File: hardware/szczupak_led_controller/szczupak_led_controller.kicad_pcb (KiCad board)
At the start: 4 copper layers, 123 parts, among them IC1 STM32G0B1CBT6, IC2 SN65HVD230DR, IC3 TLV75533PDBVR, J1 Conn_01x05, J10 XT60PW-M, J2 USB4110-GF-A, J3 CAN_CONN, J4 43650-0200, J5 43650-0300, J6 CAN_CONN, J7 Conn_EXT, J8 XT60PW-M, J9 XT60PW-M, Q1 AO4407A, Q2 AO3401A, Q3 2N7002, Q4 2N7002, Q5 2N7002, U1 USBLC6-2SC6, U3 3568

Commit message: #8 Finished initial component placement on pcb
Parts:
- removed C23, C35: 47pF DNP, Capacitor_SMD:C_0603_1608Metric
- removed D13: PESD1CAN,215, szczupak_led_controller:SOT95P230X110-3N
- added REF**: MountingHole_3.2mm_M3, MountingHole:MountingHole_3.2mm_M3, F.Cu at (83.5, 126.5)
- added REF**: MountingHole_3.2mm_M3, MountingHole:MountingHole_3.2mm_M3, F.Cu at (153.0, 73.0)
- added REF**: MountingHole_3.2mm_M3, MountingHole:MountingHole_3.2mm_M3, F.Cu at (85.5, 63.0)
- added REF**: MountingHole_3.2mm_M3, MountingHole:MountingHole_3.2mm_M3, F.Cu at (85.0, 85.5)
- added REF**: MountingHole_3.2mm_M3, MountingHole:MountingHole_3.2mm_M3, F.Cu at (164.0, 126.0)
- added REF**: MountingHole_3.2mm_M3, MountingHole:MountingHole_3.2mm_M3, F.Cu at (153.0, 95.5)
- C21, C24, C29, C30, C33, C34: moved to F.Cu
- C22, C5, F2, F3, F4, R23, R24, R25, R26: moved to B.Cu
- J7: footprint Connector_PinHeader_2.54mm:PinHeader_1x08_P2.54mm_Vertical -> Connector_PinHeader_2.54mm:PinHeader_1x10_P2.54mm_Vertical
- moved R14 268.4 mm to (86.5, 98.5), turned to -90 degrees
- moved IC3 266.4 mm to (101.6, 107.1), turned to -90 degrees
- moved D6 265.8 mm to (96.0, 102.5), turned to 180 degrees
- moved D9 265.5 mm to (96.1, 106.0), turned to 180 degrees
- moved J7 258.9 mm to (86.4, 53.0), turned to 90 degrees
- moved C16 258.3 mm to (96.0, 93.7), turned to -90 degrees
- moved C15 256.5 mm to (94.0, 93.7), turned to -90 degrees
- moved C10 256.1 mm to (100.6, 102.1), turned to 90 degrees
- moved R26 255.7 mm to (102.0, 57.5), turned to 90 degrees
- moved C6 255.7 mm to (102.8, 102.1), turned to 90 degrees
- moved C7 253.7 mm to (105.6, 108.6)
- moved C8 253.6 mm to (105.6, 111.1)
- moved R25 253.1 mm to (104.5, 57.5), turned to 90 degrees
- moved D3 252.4 mm to (113.0, 110.7), turned to 90 degrees
- moved D10 248.6 mm to (116.0, 110.7), turned to 90 degrees
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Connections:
- C15 pad 1: +3.3V -> unconnected-(C15-Pad1)
- C15 pad 2: GND -> unconnected-(C15-Pad2)
- C16 pad 1: +3.3V -> unconnected-(C16-Pad1)
- C16 pad 2: GND -> unconnected-(C16-Pad2)
- C5 pad 1: /02_mcu/NRST -> /NRST
- IC1 pad 10: /02_mcu/NRST -> /NRST
- IC1 pad 36: /02_mcu/SWCLK_BOOT0 -> /SWCLK_BOOT0
- J1 pad 1: /02_mcu/SWCLK_BOOT0 -> /SWCLK_BOOT0
- J1 pad 4: /02_mcu/NRST -> /NRST
- J7 pad 3: /USART1_TX -> /SWCLK_BOOT0
- J7 pad 4: /USART1_RX -> /NRST
- J7 pad 5: /I2C1_SDA -> /USART1_TX
- J7 pad 6: /I2C1_SCL -> /USART1_RX
- J7 pad 7: /GPIO_EXT -> /I2C1_SDA
- J7 pad 8: /PWM_EXT -> /I2C1_SCL
- Q4 pad 1: GND -> Net-(Q4-Pad1)
- R1 pad 2: /02_mcu/NRST -> /NRST
- R2 pad 1: /02_mcu/SWCLK_BOOT0 -> /SWCLK_BOOT0
- R32 pad 2: GND -> Net-(Q4-Pad1)
- R34 pad 2: GND -> Net-(Q4-Pad1)
- R7 pad 1: /ADC_LED1 -> Net-(FL1-OUT)
- R7 pad 2: Net-(FL1-OUT) -> /ADC_LED1
- S1 pad 2: /02_mcu/SWCLK_BOOT0 -> /SWCLK_BOOT0
- S1 pad 3: /02_mcu/SWCLK_BOOT0 -> /SWCLK_BOOT0
- S2 pad 1: /02_mcu/NRST -> /NRST
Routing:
- net (no net): track 1.50 -> 0.00 mm

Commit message: #8 Added routing for usb and mcu. Started pouring of power elements
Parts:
- C22, C5, R23, R24: moved to F.Cu
- R12, R13: moved to B.Cu
- moved R12 13.4 mm to (120.1, 68.2)
- moved R13 13.4 mm to (120.1, 66.6)
- moved R24 10.2 mm to (91.8, 64.9), turned to -90 degrees
- moved R23 8.25 mm to (91.8, 68.2), turned to -90 degrees
- moved JP3 8.17 mm to (79.5, 120.8), turned to 0 degrees
- moved C3 6.53 mm to (108.7, 76.0)
- moved C4 6.53 mm to (108.7, 78.0)
- moved C20 5.62 mm to (77.8, 85.5)
- moved C29 4.25 mm to (130.0, 76.8)
- moved C24 4.23 mm to (130.0, 98.8)
- moved C30 4.14 mm to (132.0, 75.0)
- moved C21 3.93 mm to (132.0, 97.5)
- moved C33 3.75 mm to (130.0, 54.0)
- moved C9 3.64 mm to (108.8, 63.9), turned to 90 degrees
- moved R2 3.58 mm to (97.7, 77.4), turned to -90 degrees
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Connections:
- net Net-(D1-K) renamed /02_mcu/LED_STATUS_R
- net Net-(D2-K) renamed /02_mcu/LED_FAULT_R
- net Net-(FL1-OUT) renamed /04_power_output/ADC_R1
- net Net-(FL2-OUT) renamed /04_power_output/ADC_R2
- net Net-(FL3-OUT) renamed /04_power_output/ADC_R3
- net Net-(JP2-A) renamed /03_interfaces/CAN_SHIELD_1
- net Net-(JP3-A) renamed /03_interfaces/CAN_SHIELD_2
- net Net-(Q3-Pad1) renamed /04_power_output/PWM_LED1_GATE
- net Net-(Q4-Pad1) renamed /04_power_output/PWM_LED2_GATE
- net Net-(Q5-Pad1) renamed /04_power_output/PWM_LED3_GATE
- C15 pad 1: unconnected-(C15-Pad1) -> +3.3V
- C15 pad 2: unconnected-(C15-Pad2) -> GND
- C16 pad 1: unconnected-(C16-Pad1) -> +3.3V
- C16 pad 2: unconnected-(C16-Pad2) -> GND
- J7 pad 10: /PWM_EXT -> /GPIO_EXT
- J7 pad 9: /GPIO_EXT -> /PWM_EXT
- S1 pad 5: GND -> unconnected-(S1-GROUND-Pad5)
- S2 pad 5: GND -> unconnected-(S2-GROUND-Pad5)
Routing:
- net /NRST: track 0.00 -> 65.9 mm, vias 0 -> 2
- net /PWM_LED1: track 0.00 -> 65.1 mm, vias 0 -> 2
- net /SWCLK_BOOT0: track 0.00 -> 64.8 mm, vias 0 -> 4
- net /03_interfaces/CAN_P: track 0.00 -> 46.8 mm, vias 0 -> 5
- net /03_interfaces/CAN_N: track 0.00 -> 45.1 mm
- net /PWM_LED2: track 0.00 -> 44.5 mm, vias 0 -> 2
- net /ADC_LED1: track 0.17 -> 40.2 mm
- net /02_mcu/LED_STATUS: track 0.24 -> 34.3 mm, vias 0 -> 2
- net /I2C1_SDA: track 0.00 -> 32.3 mm, vias 0 -> 2
- net /I2C1_SCL: track 0.00 -> 31.8 mm, vias 0 -> 2
- net /03_interfaces/CAN_SPLIT: track 0.00 -> 31.3 mm, vias 0 -> 1
- net /02_mcu/LED_FAULT: track 0.00 -> 31.2 mm, vias 0 -> 2
- net /CAN_TX: track 0.00 -> 31.1 mm
- net /USART1_TX: track 0.00 -> 29.8 mm, vias 0 -> 1
- net /USART1_RX: track 0.00 -> 28.9 mm, vias 0 -> 1
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- added copper zone on B.Cu, net +3.3V
- added copper zone on F.Cu, net +3.3V
- added copper zone on F.Cu, net /01_power_input/12V_FUSE
- added copper zone on F.Cu, net /01_power_input/5V_FUSE
- added copper zone on F.Cu, net /01_power_input/5V_IN
- added copper zone on F.Cu, net /01_power_input/5V_PROT
- added copper zone on F.Cu, net /01_power_input/Q1_GATE
- added copper zone on F.Cu, net /01_power_input/Q2_GATE
- added copper zone on F.Cu, net /04_power_output/12V_CH3
- added copper zone on F.Cu, net /USB_5V
- added copper zone on B.Cu, net GND
- added copper zone on In1.Cu, net GND
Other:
- board outline added: 100 x 83 mm

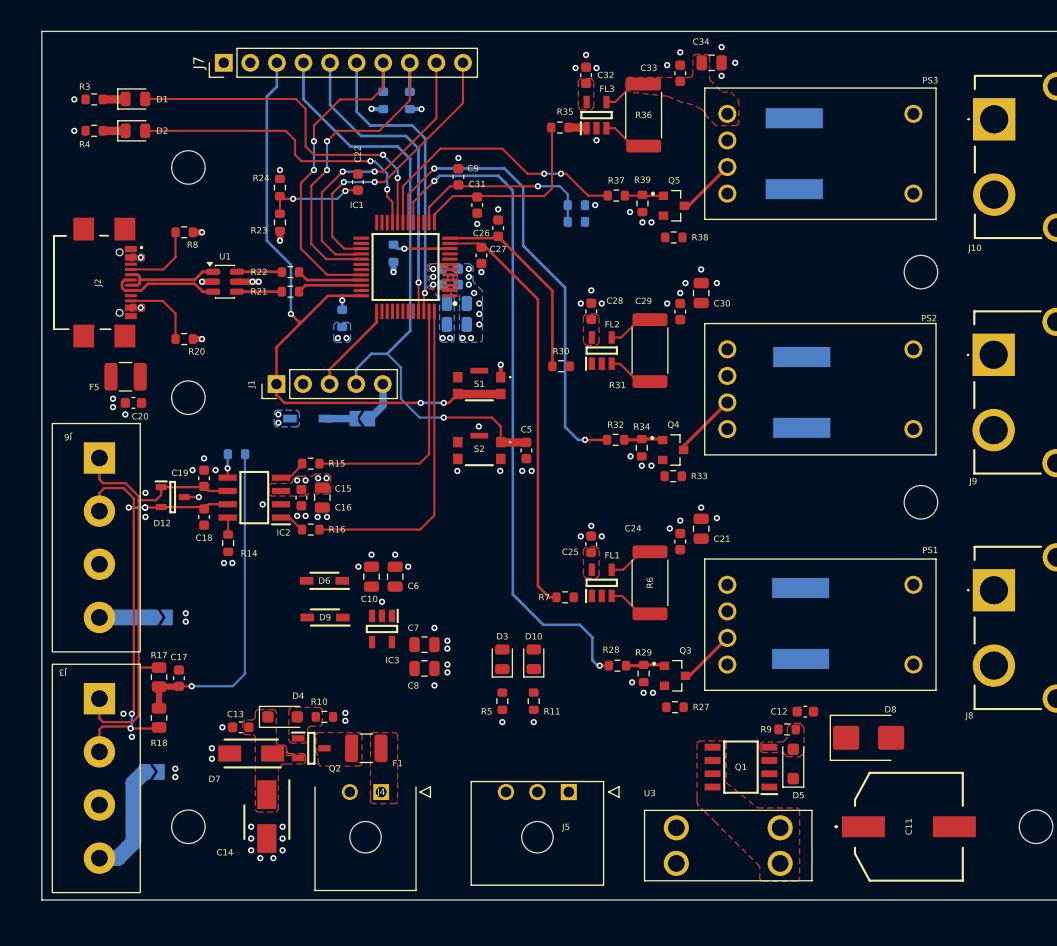
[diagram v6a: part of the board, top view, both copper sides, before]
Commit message: #8 Created first version of pcb design
All KiCad tests passed, so pcb is ready to review
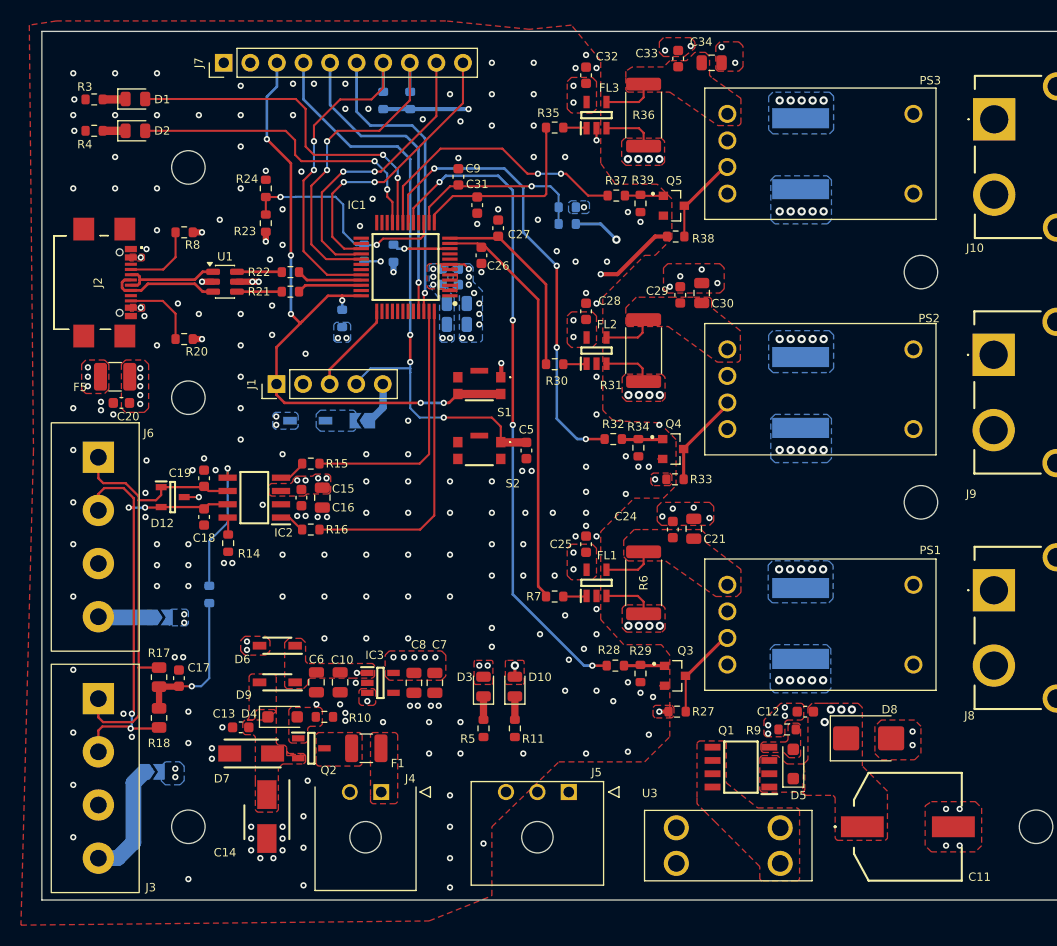
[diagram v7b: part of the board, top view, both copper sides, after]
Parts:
- C22: moved to B.Cu
- moved R19 13.6 mm to (85.0, 103.8), turned to 90 degrees
- moved C6 12.6 mm to (95.2, 112.2), turned to -90 degrees
- moved C10 10.5 mm to (97.5, 112.2), turned to -90 degrees
- moved J6 9.40 mm to (73.9, 98.4)
- moved J3 9.40 mm to (73.9, 121.5)
- moved D9 7.70 mm to (91.5, 112.2)
- moved D6 7.66 mm to (91.5, 108.7)
- moved C22 6.83 mm to (99.8, 71.2), turned to -90 degrees
- moved IC3 5.15 mm to (101.3, 112.2), turned to 0 degrees
- moved C7 3.78 mm to (106.5, 112.2), turned to -90 degrees
- moved D10 3.16 mm to (114.2, 112.6)
- moved D3 3.16 mm to (111.2, 112.6)
- moved R11 3.16 mm to (114.2, 116.6)
- moved R5 3.16 mm to (111.2, 116.6)
- moved C8 1.71 mm to (104.5, 112.2), turned to -90 degrees
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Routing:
- net +3.3V: track 4.76 -> 256.2 mm, vias 15 -> 30
- net /12V_LED: track 0.00 -> 56.6 mm, vias 0 -> 21
- net /01_power_input/USB_5V_FUSE: track 0.00 -> 39.9 mm, vias 0 -> 5
- net /USB_5V: track 3.01 -> 36.6 mm, vias 5 -> 10
- net /03_interfaces/CAN_SPLIT: track 31.3 -> 13.8 mm
- net /ADC_USB: track 9.57 -> 21.9 mm
- net /03_interfaces/CAN_VREF: track 2.14 -> 12.9 mm
- net GND: track 4.20 -> 10.4 mm, vias 108 -> 252
- net /01_power_input/+VIN_LOGIC: track 0.00 -> 5.70 mm, vias 0 -> 2
- net /04_power_output/RCD_PWM_CH3: track 5.23 -> 8.58 mm
- net /04_power_output/RCD_PWM_CH1: track 5.50 -> 8.74 mm
- net /04_power_output/RCD_PWM_CH2: track 6.27 -> 9.08 mm
- net /02_mcu/3V3_PROG_D: track 2.80 -> 0.00 mm
- net /04_power_output/ADC_R2: track 0.00 -> 2.46 mm
- net /04_power_output/ADC_R1: track 0.00 -> 2.25 mm
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- added copper zone on F.Cu, net /01_power_input/+VIN_LOGIC
- added copper zone on In2.Cu, net /01_power_input/12V_IN
- added copper zone on F.Cu, net /01_power_input/USB_5V_FUSE
- added copper zone on B.Cu, net /02_mcu/3V3_PROG_D
- added copper zone on F.Cu, net /04_power_output/12V_CH1
- added copper zone on B.Cu, net /04_power_output/12V_CH1_SH
- added copper zone on F.Cu, net /04_power_output/12V_CH1_SH
- added copper zone on In2.Cu, net /04_power_output/12V_CH1_SH
- added copper zone on F.Cu, net /04_power_output/12V_CH2
- added copper zone on B.Cu, net /04_power_output/12V_CH2_SH
- added copper zone on F.Cu, net /04_power_output/12V_CH2_SH
- added copper zone on In2.Cu, net /04_power_output/12V_CH2_SH
- added copper zone on B.Cu, net /04_power_output/12V_CH3_SH
- added copper zone on F.Cu, net /04_power_output/12V_CH3_SH
- added copper zone on In2.Cu, net /04_power_output/12V_CH3_SH
- added copper zone on In2.Cu, net /04_power_output/LED1+
- added copper zone on In2.Cu, net /04_power_output/LED1-
- added copper zone on In2.Cu, net /04_power_output/LED2+
- added copper zone on In2.Cu, net /04_power_output/LED2-
- added copper zone on In2.Cu, net /04_power_output/LED3+
- added copper zone on In2.Cu, net /04_power_output/LED3-
- added copper zone on B.Cu, net /12V_LED
- added copper zone on F.Cu, net /12V_LED
- added copper zone on In2.Cu, net /12V_LED
- added copper zone on F.Cu, net GND
- added copper zone on In2.Cu, net GND
